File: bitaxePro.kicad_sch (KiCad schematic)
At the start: 101 parts, among them IC1 BM1387, IC2 BM1387, IC3 TCR2EF18, IC4 TCR2EF18, J1 Conn_01x01, J2 Conn_01x01, J3 Conn_01x05, J4 Conn_01x02, J5 Conn_01x03, Y1 25MHz

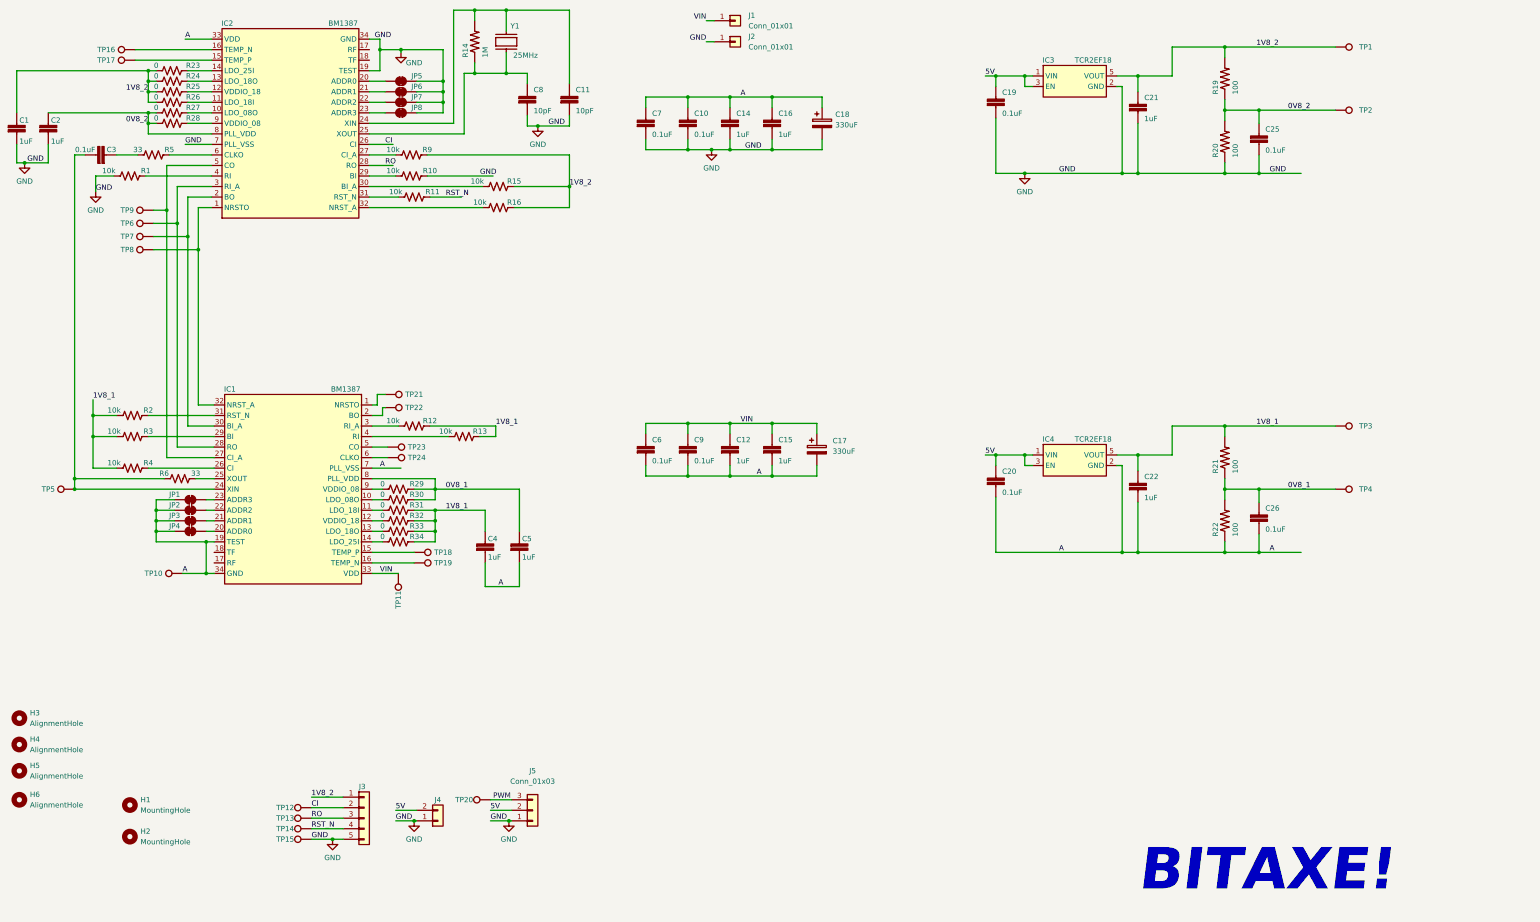
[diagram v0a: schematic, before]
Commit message: made separate symbols for BM1397 in mode0 and mode1
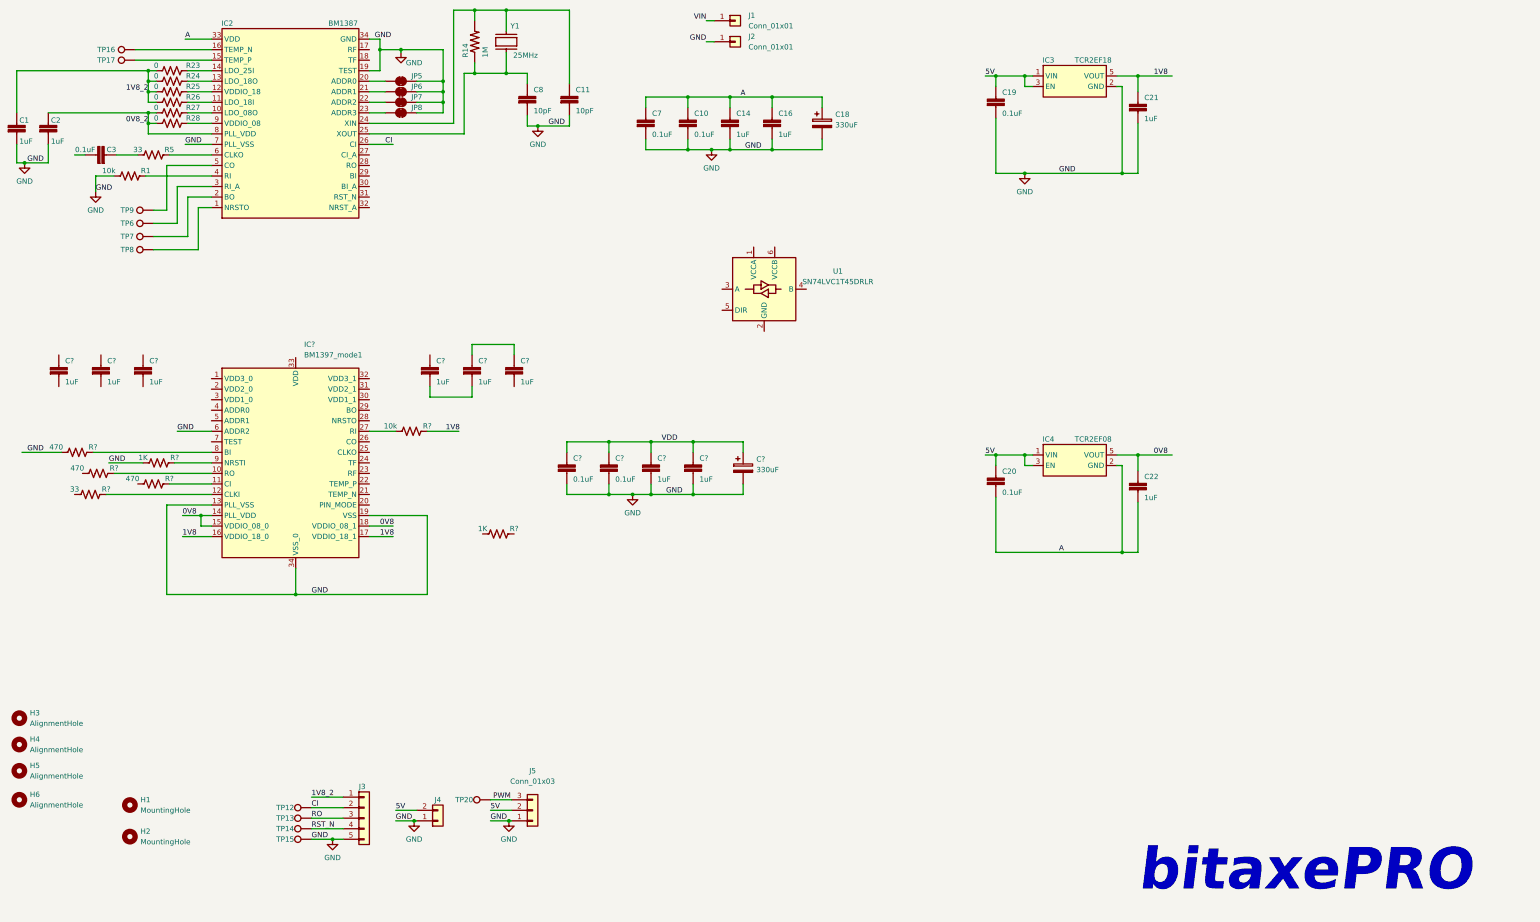
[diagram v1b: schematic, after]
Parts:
- removed C12, C15: 587-5514-1-ND, DayMiner:C0402, symbol DayMiner-eagle-import:CAP0402
- removed C17: 330uF, Capacitor_Tantalum_SMD:CP_EIA-7343-31_Kemet-D_Pad2.25x2.55mm_HandSolder, symbol Device:C_Polarized
- removed C25, C26, C6, C9: 311-3342-1-ND, DayMiner:C0402, symbol DayMiner-eagle-import:CAP0402
- removed C4, C5: 1uF, DayMiner:C0402, symbol DayMiner-eagle-import:CAP0402
- removed IC1: BM1387, DayMiner:SON45P800X800X70-33T645X800N, symbol dayminer:BM1387
- removed JP1, JP2, JP3, JP4: SolderJumper_2_Bridged, Jumper:SolderJumper-2_P1.3mm_Bridged2Bar_RoundedPad1.0x1.5mm, symbol Jumper:SolderJumper_2_Bridged
- removed R10, R11, R12, R13, R15, R16, R2, R3, R4, R9: 10k, DayMiner:R0402, symbol Device:R_US
- removed R19, R20, R21, R22: 100, DayMiner:R0402, symbol DayMiner-eagle-import:RESISTOR0402-RES
- removed R29, R30, R31, R32, R33, R34: 0, DayMiner:R0402, symbol Device:R_US
- removed R6: 33, DayMiner:R0402, symbol Device:R_US
- removed TP1, TP10, TP11, TP18, TP19, TP2, TP21, TP22, TP23, TP24, TP3, TP4, TP5: TestPoint, TestPoint:TestPoint_Pad_D1.5mm, symbol Connector:TestPoint
- added C? (x8): 587-5514-1-ND, DayMiner:C0402, symbol DayMiner-eagle-import:CAP0402
- added C? (x2): 311-3342-1-ND, DayMiner:C0402, symbol DayMiner-eagle-import:CAP0402
- added C?: 330uF, Capacitor_Tantalum_SMD:CP_EIA-7343-31_Kemet-D_Pad2.25x2.55mm_HandSolder, symbol Device:C_Polarized
- added IC?: BM1397_mode1, symbol bitaxe:BM1397_mode1
- added R? (x2): 1K, DayMiner:R0402, symbol Device:R_US
- added R?: 10k, DayMiner:R0402, symbol Device:R_US
- added R? (x3): 470, DayMiner:R0402, symbol Device:R_US
- added R?: 33, DayMiner:R0402, symbol Device:R_US
- added U1: SN74LVC1T45DRLR, DayMiner:SN74LVC1T45DRLR, symbol Logic_LevelTranslator:SN74LVC1T45DBV
- IC4: value TCR2EF18 -> TCR2EF08; DK TCR2EF18LM(CTCT-ND -> TCR2LF08LM(CTCT-ND; PARTNO TCR2EF18,LM(CT -> TCR2LF08,LM(CT
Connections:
- net 1V8_2: no longer C21.1, IC3.5 (VOUT)
- net GND: now also C?.2, C?.2, C?.2, C?.2, C?.2, IC?.13 (PLL_VSS), IC?.19 (VSS), IC?.34 (VSS_0), IC?.6 (ADDR2), R?.1, R?.1
- net RO: no longer IC2.28 (RO)
- net 1V8_1 renamed 0V8
- net 0V8: now also IC?.14 (PLL_VDD), IC?.15 (VDDIO_08_0), IC?.18 (VDDIO_08_1)
- new net: IC?.9 (NRSTI), R?.2
- new net: IC?.27 (RI), R?.1
- new net: IC?.8 (BI), R?.2
- new net: C?.2, C?.2
- new net: C?.1, C?.1
- new net: IC?.12 (CLKI), R?.2
- new net: IC?.11 (CI), R?.2
- new net: IC?.10 (RO), R?.2
- new net 1V8: C21.1, IC3.5 (VOUT), IC?.16 (VDDIO_18_0), IC?.17 (VDDIO_18_1), R?.2
- new net VDD: C?.1, C?.1, C?.1, C?.1, C?.1
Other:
- note added: "bitaxePRO"
- note removed: "BITAXE!"

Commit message: schematic pretty much done
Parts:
- removed C10, C7: 311-3342-1-ND, DayMiner:C0402, symbol DayMiner-eagle-import:CAP0402
- removed C11: 311-3607-1-ND, DayMiner:C0402, symbol DayMiner-eagle-import:CAP0402
- removed C18: 330uF, Capacitor_Tantalum_SMD:CP_EIA-7343-31_Kemet-D_Pad2.25x2.55mm_HandSolder, symbol Device:C_Polarized
- removed C3: 0.1uF, DayMiner:C0402, symbol eagle_import:CAP0402
- removed C? (x3): 587-5514-1-ND, DayMiner:C0402, symbol DayMiner-eagle-import:CAP0402
- removed IC2: BM1387, DayMiner:SON45P800X800X70-33T645X800N, symbol dayminer:BM1387
- removed IC3: TCR2EF18, DayMiner:TCR2EF18, symbol DayMiner-eagle-import:MIC5317
- removed IC4: TCR2EF08, DayMiner:TCR2EF18, symbol DayMiner-eagle-import:MIC5317
- removed JP5, JP6, JP7, JP8: SolderJumper_2_Bridged, Jumper:SolderJumper-2_P1.3mm_Bridged2Bar_RoundedPad1.0x1.5mm, symbol Jumper:SolderJumper_2_Bridged
- removed R1: 10k, DayMiner:R0402, symbol Device:R_US
- removed R14: 311-1.00MLRCT-ND, DayMiner:R0402, symbol DayMiner-eagle-import:RESISTOR0402-RES
- removed R23, R24, R25, R26, R27, R28: 0, DayMiner:R0402, symbol Device:R_US
- removed R5: 33, DayMiner:R0402, symbol Device:R_US
- removed R?: 1K, DayMiner:R0402, symbol Device:R_US
- removed TP16, TP17: TestPoint, TestPoint:TestPoint_Pad_D1.5mm, symbol Connector:TestPoint
- removed U1: SN74LVC1T45DRLR, DayMiner:SN74LVC1T45DRLR, symbol Logic_LevelTranslator:SN74LVC1T45DBV
- removed Y1: 25MHz, DayMiner:XRCGB25M000F2P02R0, symbol DayMiner-eagle-import:XRCGB25M000F2P02R0
- added C18, C3, C4, C5, C6, C? (x3): 587-5514-1-ND, DayMiner:C0402, symbol DayMiner-eagle-import:CAP0402
- added C? (x6): 311-3342-1-ND, DayMiner:C0402, symbol DayMiner-eagle-import:CAP0402
- added JP1, JP2: SolderJumper_2_Open, Jumper:SolderJumper-2_P1.3mm_Open_RoundedPad1.0x1.5mm, symbol Jumper:SolderJumper_2_Open
- added JP3: SolderJumper_2_Bridged, Jumper:SolderJumper-2_P1.3mm_Bridged2Bar_RoundedPad1.0x1.5mm, symbol Jumper:SolderJumper_2_Bridged
- added TP1, TP10, TP11, TP2, TP3, TP4, TP5: TestPoint, TestPoint:TestPoint_Pad_D1.5mm, symbol Connector:TestPoint
- added U2: oscillator, DayMiner:O 25,0-JO32-B-1V3-1-T1-LF, symbol bitaxe:oscillator
- added U? (x2): MCP1824, Package_TO_SOT_SMD:SOT-23-5, symbol bitaxe:MCP1824
- added U? (x3): SN74LVC1T45DRLR, Package_TO_SOT_SMD:SOT-23-6, symbol bitaxe:SN74LVC1T45DBV
- C1: value 1uF -> 311-3342-1-ND; DK 587-5514-1-ND -> 1292-1639-1-ND
- C2: value 1uF -> 587-5514-1-ND
- C8: value 311-3607-1-ND -> 587-5514-1-ND; DK 399-C0402C100K5RAC7867CT-ND -> 587-5514-1-ND
- R3, R4: renamed from R?; value 470 -> 0
- gave numbers to parts that had none: 13
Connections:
- net 0V8_2 is gone; now on net GND: C2.1
- net VIN is gone; now on net VDD: J1.1 (Pin_1)
- net 0V8: now also C16.1, C4.1, TP11.1, U?.5 (VOUT)
- net 1V8: now also C1.2, C14.1, C5.1, C?.1, C?.1, C?.1, C?.1, C?.1, C?.1, TP10.1, U2.4 (VIN), U?.5 (VOUT), U?.6 (VCCB), U?.6 (VCCB), U?.6 (VCCB)
- net 5V: now also U?.1 (VIN), U?.1 (VIN), U?.3 (EN), U?.3 (EN)
- net CI: now also R4.1, U?.4 (B); no longer J3.2 (Pin_2), TP12.1
- net GND: now also C1.1, C20.2, C22.2, C18.2, C4.2, C5.2, C?.2, C?.2, C?.2, C?.2, C?.2, C?.2, C?.2, C?.2, C?.2, JP1.1 (A), JP2.1 (A), JP3.1 (A), U2.2 (GND), U?.2 (GND), U?.2 (GND), U?.2 (GND), U?.2 (GND), U?.2 (GND), U?.5 (DIR); no longer C1.2, C2.2, C8.2, IC1.6 (ADDR2)
- net RO: now also R3.1, U?.4 (B); no longer J3.3 (Pin_3), TP13.1
- net RST_N: now also IC1.9 (NRSTI), R5.2, U?.4 (B); no longer J3.4 (Pin_4), TP14.1
- net VDD: now also C12.1, C8.2, IC1.33 (VDD)
- net at C8.1: now also IC1.1 (VDD3_0), C6.2
- net at TP8.1: now also IC1.21 (TEMP_N)
- net at TP7.1: now also IC1.22 (TEMP_P)
- net at TP6.1: now also IC1.25 (CLKO)
- net at TP9.1: now also IC1.20 (PIN_MODE)
- net at C12.2: now also C15.1, IC1.32 (VDD3_1); no longer C15.2
- net at C17.1: now also C15.2, IC1.31 (VDD2_1); no longer C15.1
- net at C17.2: now also IC1.30 (VDD1_1), C18.1
- net at R2.1: now also TP2.1, U2.3 (OUT)
- net at IC1.2 (VDD2_0): now also C3.2, C6.1
- net at IC1.26 (CO): now also TP5.1
- net at IC1.28 (NRSTO): now also TP4.1
- net at IC1.29 (BO): now also TP3.1
- net at IC1.3 (VDD1_0): now also C2.2, C3.1
- net at IC1.4 (ADDR0): now also JP1.2 (B)
- net at IC1.5 (ADDR1): now also JP2.2 (B)
- net 1V8_2 renamed VCCIO
- net VCCIO: now also C?.1, C?.1, C?.1, U?.1 (VCCA), U?.1 (VCCA), U?.1 (VCCA), U?.5 (DIR), U?.5 (DIR); no longer C1.1
- removed net A: C14.1, C16.1, C20.2, C22.2
- new net: IC1.6 (ADDR2), JP3.2 (B)
- new net: TP1.1, U2.1 (EN)
- new net RST: J3.4 (Pin_4), TP14.1, U?.3 (A)
- new net RX: J3.3 (Pin_3), TP13.1, U?.3 (A)
- new net TX: J3.2 (Pin_2), TP12.1, U?.3 (A)
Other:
- moved on the sheet: C10, C11, C12, C13, C15, C17, C19, C20, C21, C22, C7, C9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

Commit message: added an ESP32-C3 to try out. Added a NCT218
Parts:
- added C32: 1000pF, DayMiner:C0402, symbol DayMiner-eagle-import:CAP0402
- added C33: 311-3342-1-ND, DayMiner:C0402, symbol DayMiner-eagle-import:CAP0402
- added R10, R11: (no value), Resistor_SMD:R_0402_1005Metric, symbol DayMiner-eagle-import:RESISTOR0402-RES
- added R7: 10K, DayMiner:R0402, symbol Device:R_US
- added R8, R9: 100, Resistor_SMD:R_0402_1005Metric, symbol DayMiner-eagle-import:RESISTOR0402-RES
- added TP16, TP17, TP18, TP19: TestPoint, TestPoint:TestPoint_Pad_D1.5mm, symbol Connector:TestPoint
- added U7: ESP32-C3-DEVKITC-02, DayMiner:XCVR_ESP32-C3-DEVKITC-02, symbol bitaxe:ESP32-C3-DEVKITC-02
- added U8: NCT218, Package_DFN_QFN:DFN-8_2x2mm_P0.5mm, symbol dayminer:NCT218
- IC1: footprint (none) -> DayMiner:SON45P800X800X70-33T645X800N
- gave numbers to parts that had none: 14
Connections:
- net 5V: now also U7.13 (5V), U7.14 (5V)
- net CI: now also TP17.1
- net GND: now also C33.2, U7.1 (GND), U7.10 (GND), U7.15 (GND), U7.16 (GND), U7.17 (GND), U7.20 (GND), U7.23 (GND), U7.25 (GND), U7.30 (GND), U7.5 (GND), U8.5 (GND)
- net RO: now also TP16.1
- net RST: now also U7.24 (GPIO10)
- net RST_N: now also TP18.1
- net RX: now also U7.27 (GPIO2)
- net TX: now also U7.26 (GPIO3)
- net VCCIO: now also C33.1, R10.2, R11.2, R7.2, U7.2 (3V3), U7.3 (3V3), U8.1 (VDD)
- net TEMP_P: now reaches IC1.22 (TEMP_P), TP7.1
- net TEMP_P: now also R9.1
- net TEMP_N: now reaches IC1.21 (TEMP_N), TP8.1
- net TEMP_N: now also R8.2
- net PWM renamed FAN_TACH
- net FAN_TACH: now also R7.1, U7.6 (GPIO4)
- new net: C32.2, R8.1, U8.3 (D-)
- new net: TP19.1, U7.4 (RST)
- new net: C32.1, R9.2, U8.2 (D+)
- new net SCL: R10.1, U7.19 (GPIO18), U8.8 (SCL)
- new net SDA: R11.1, U7.18 (GPIO19), U8.7 (SDA)
- new net TEMP_ALRT: U7.12 (GPIO9), U8.6 (ALERT)
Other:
- note added: "bitaxeMAX"
- note removed: "bitaxePRO"
- moved on the sheet: J5, TP7, TP8

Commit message: lots of routing
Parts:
- removed R10, R11: (no value), Resistor_SMD:R_0402_1005Metric, symbol DayMiner-eagle-import:RESISTOR0402-RES
- added R10, R11: 1K, DayMiner:R0402, symbol Device:R_US
- added TP21, TP22, TP23: TestPoint, TestPoint:TestPoint_Pad_D1.5mm, symbol Connector:TestPoint
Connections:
- net CI: now also J3.2 (Pin_2), TP12.1; no longer TP17.1
- net RO: now also J3.3 (Pin_3), TP13.1; no longer TP16.1
- net RST: now also TP18.1; no longer J3.4 (Pin_4), TP14.1
- net RST_N: now also J3.4 (Pin_4), TP14.1; no longer TP18.1
- net RX: now also TP17.1; no longer J3.3 (Pin_3), TP13.1
- net SCL: now also R10.1, TP21.1
- net SDA: now also R11.1, TP22.1
- net TEMP_ALRT: now also TP23.1
- net TX: now also TP16.1; no longer J3.2 (Pin_2), TP12.1
- net VCCIO: now also R10.2, R11.2
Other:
- moved on the sheet: R1, R3, R4, R5, TP17

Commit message: updated part numbers and generated BOM
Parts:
- R1: DK (none) -> CR0402-JW-471GLFCT-ND
- R10, R11, R5: DK (none) -> YAG2306CT-ND
- R3, R4: DK (none) -> RMCF0402ZT0R00CT-ND
- R7: DK (none) -> YAG1346CT-ND
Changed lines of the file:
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@@
       (effects (font (size 1.27 1.27)) hide)
     )
-    (property "DK" "" (id 4) (at 374.65 128.905 0)
+    (property "DK" "YAG2306CT-ND" (id 4) (at 374.65 128.905 0)
       (effects (font (size 1.27 1.27)) hide)
     )
@@
       (effects (font (size 1.27 1.27)) hide)
     )
-    (property "DK" "" (id 4) (at 49.53 82.55 0)
+    (property "DK" "YAG2306CT-ND" (id 4) (at 49.53 82.55 0)
       (effects (font (size 1.27 1.27)) hide)
     )
@@
       (effects (font (size 1.27 1.27)) hide)
     )
-    (property "DK" "" (id 4) (at 85.725 74.295 0)
+    (property "DK" "CR0402-JW-471GLFCT-ND" (id 4) (at 85.725 74.295 0)
       (effects (font (size 1.27 1.27)) hide)
     )
@@
       (effects (font (size 1.27 1.27)) hide)
     )
-    (property "DK" "" (id 4) (at 85.725 81.915 0)
+    (property "DK" "RMCF0402ZT0R00CT-ND" (id 4) (at 85.725 81.915 0)
       (effects (font (size 1.27 1.27)) hide)
     )
@@
       (effects (font (size 1.27 1.27)) hide)
     )
-    (property "DK" "" (id 4) (at 296.545 113.665 0)
+    (property "DK" "YAG1346CT-ND" (id 4) (at 296.545 113.665 0)
       (effects (font (size 1.27 1.27)) hide)
     )
@@
       (effects (font (size 1.27 1.27)) hide)
     )
-    (property "DK" "" (id 4) (at 75.565 79.375 0)
+    (property "DK" "RMCF0402ZT0R00CT-ND" (id 4) (at 75.565 79.375 0)
       (effects (font (size 1.27 1.27)) hide)
     )
@@
       (effects (font (size 1.27 1.27)) hide)
     )
-    (property "DK" "" (id 4) (at 382.905 128.905 0)
-      (effects (font (size 1.27 1.27)) hide)
-    )
+    (property "DK" "YAG2306CT-ND" (id 4) (at 382.905 128.905 0)
+      (effects (font (size 1.27 1.27)) hide)
+    )
